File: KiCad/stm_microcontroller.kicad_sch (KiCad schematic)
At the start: 21 parts, among them J5 USB_C_Receptacle_USB2.0_14P, SW1 SW_Push, SW2 SW_Push, U1 STM32F103C8Tx, Y1 8Mhz

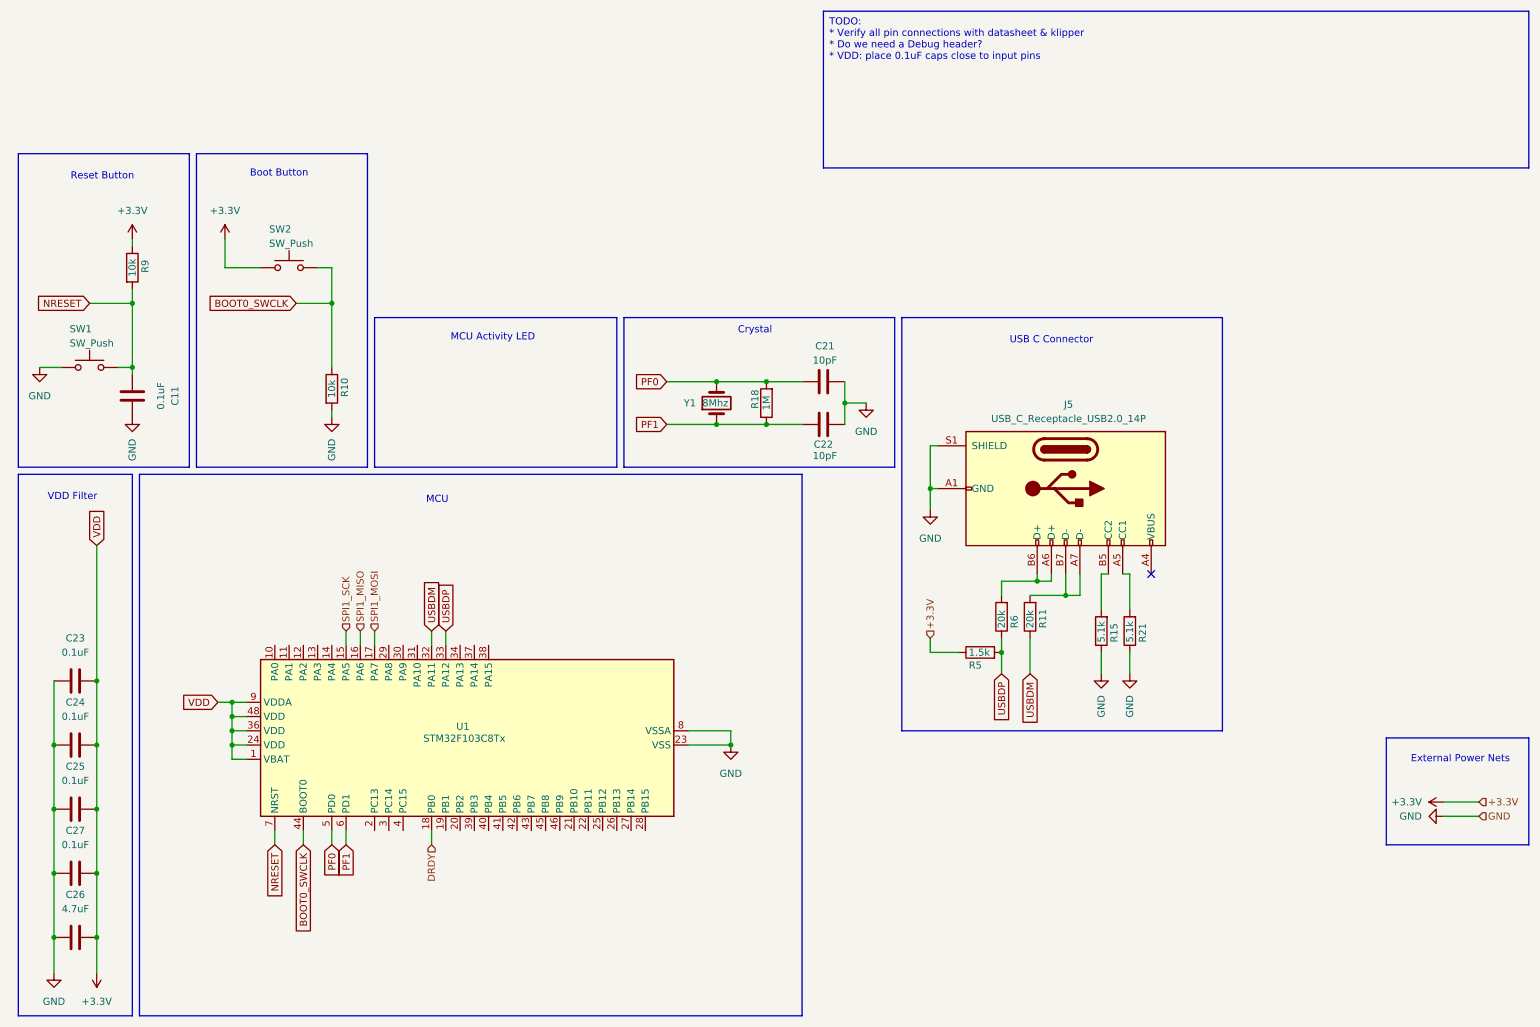
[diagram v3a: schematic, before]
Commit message: Update Switch Footprints
Update switch schematic and footprint to match the actual part being used
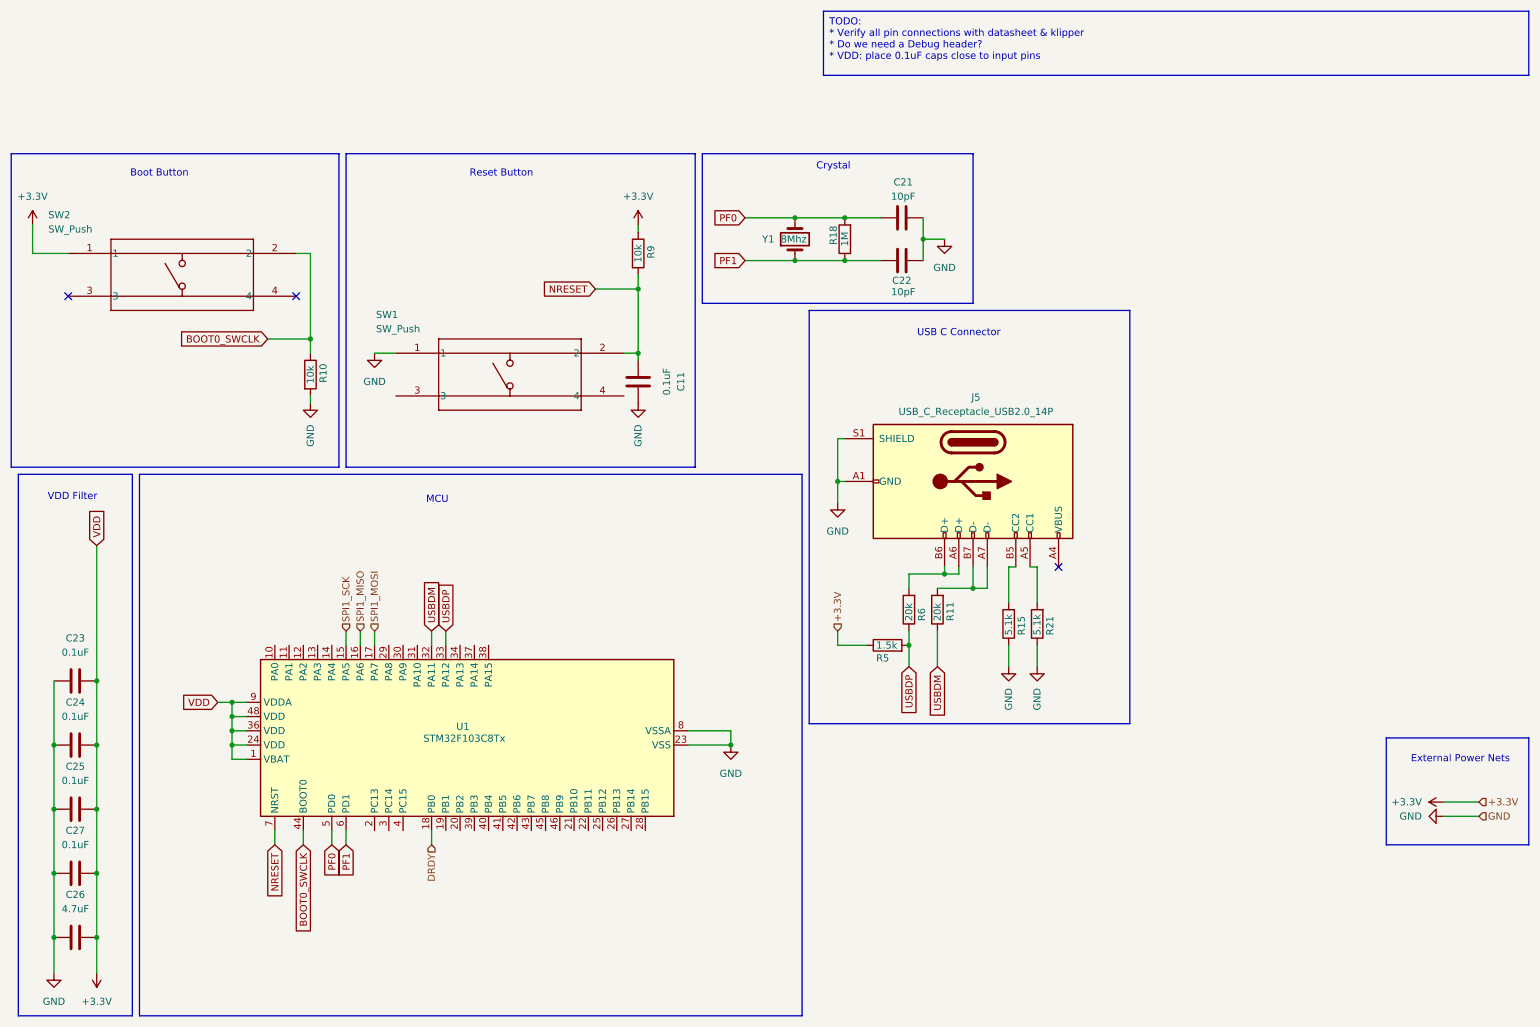
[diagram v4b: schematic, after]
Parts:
- J5: footprint Connector_USB:USB_C_Receptacle_GCT_USB4110 -> Connector_USB:USB_C_Receptacle_GCT_USB4085
- SW1, SW2: footprint Button_Switch_SMD:SW_Push_1P1T_NO_6x6mm_H9.5mm -> SWITCH_43SMTR92LFS; symbol Switch:SW_Push -> PTS645 Switch:PTS645SM43SMTR92LFS
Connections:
- no-connect marks 1 -> 3
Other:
- note removed: "MCU Activity LED"
- moved on the sheet: C11, C21, C22, J5, R10, R11, R15, R18, R21, R5, R6, R9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

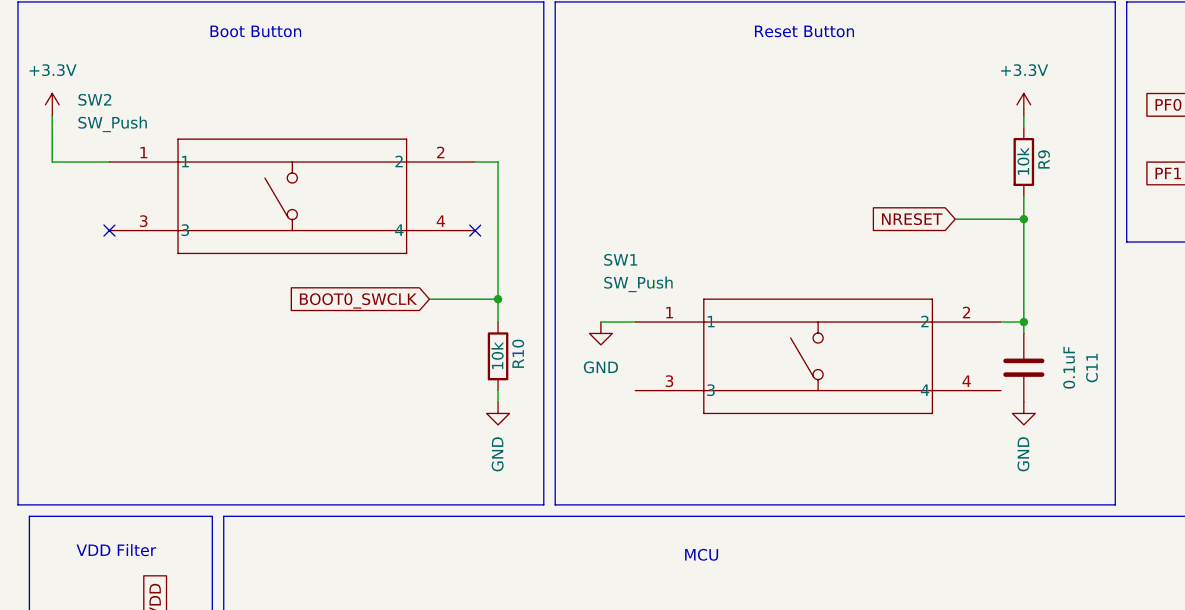
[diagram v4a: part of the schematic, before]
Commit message: Update Inductor Footprint
Update to PA4332.222NLT
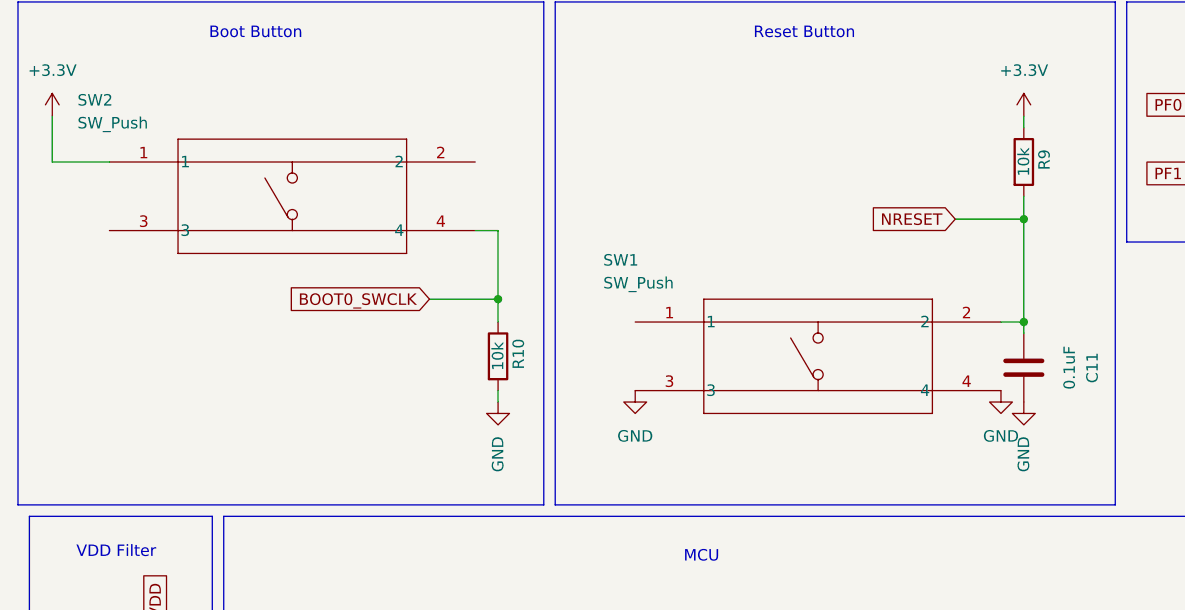
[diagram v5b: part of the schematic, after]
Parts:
- Y1: footprint Crystal:Crystal_SMD_SeikoEpson_FA238V-4Pin_3.2x2.5mm_HandSoldering -> Crystal:Crystal_SMD_Abracon_ABM3-2Pin_5.0x3.2mm
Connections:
- net BOOT0_SWCLK: now also SW2.4; no longer SW2.2
- net GND: now also SW1.3, SW1.4; no longer SW1.1
- no-connect marks 3 -> 1
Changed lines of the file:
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@@
 	)
 	(no_connect
-		(at 63.5 64.77)
-	)
-	(no_connect
-		(at 22.86 64.77)
-	)
-	(no_connect
 		(at 199.39 113.03)
 	)
@@
 	(wire
 		(pts
-			(xy 63.5 57.15) (xy 66.04 57.15)
+			(xy 63.5 64.77) (xy 66.04 64.77)
 		)
 		(stroke
@@
 	(wire
 		(pts
-			(xy 66.04 57.15) (xy 66.04 72.39)
+			(xy 66.04 64.77) (xy 66.04 72.39)
 		)
 		(stroke
@@
 	(wire
 		(pts
-			(xy 77.47 74.93) (xy 81.28 74.93)
-		)
-		(stroke
-			(width 0)
-			(type default)
-		)
-	)
-	(wire
-		(pts
 			(xy 52.07 137.16) (xy 52.07 139.7)
 		)
@@
 	)
 	(symbol
+		(lib_id "power:GND")
+		(at 121.92 82.55 0)
+		(unit 1)
+		(exclude_from_sim no)
+		(in_bom yes)
+		(on_board yes)
+		(dnp no)
+		(fields_autoplaced yes)
+		(property "Reference" "#PWR02"
+			(at 121.92 88.9 0)
+			(effects
+				(font
+					(size 1.27 1.27)
+				)
+				(hide yes)
+			)
+		)
+		(property "Value" "GND"
+			(at 121.92 87.63 0)
+			(effects
+				(font
+					(size 1.27 1.27)
+				)
+			)
+		)
+		(property "Footprint" ""
+			(at 121.92 82.55 0)
+			(effects
+				(font
+					(size 1.27 1.27)
+				)
+				(hide yes)
+			)
+		)
+		(property "Datasheet" ""
+			(at 121.92 82.55 0)
+			(effects
+				(font
+					(size 1.27 1.27)
+				)
+				(hide yes)
+			)
+		)
+		(property "Description" "Power symbol creates a global label with name \"GND\" , ground"
+			(at 121.92 82.55 0)
+			(effects
+				(font
+					(size 1.27 1.27)
+				)
+				(hide yes)
+			)
+		)
+		(pin "1"
+		)
+		(instances
+			(project "ADS1220 4-Load Cell Board"
+				(path "/5d164854-6659-4076-ba4e-df0771b4723d/50dff8a5-558b-4d50-9ac6-b993f14c2b34"
+					(reference "#PWR02")
+					(unit 1)
+				)
+			)
+		)
+	)
+	(symbol
 		(lib_id "Connector:USB_C_Receptacle_USB2.0_14P")
 		(at 184.15 97.79 270)
@@
 	(symbol
 		(lib_id "power:GND")
-		(at 77.47 74.93 0)
+		(at 81.28 82.55 0)
 		(unit 1)
 		(exclude_from_sim no)
@@
 		(fields_autoplaced yes)
 		(property "Reference" "#PWR025"
-			(at 77.47 81.28 0)
+			(at 81.28 88.9 0)
 			(effects
 				(font
@@
 		)
 		(property "Value" "GND"
-			(at 77.47 80.01 0)
+			(at 81.28 87.63 0)
 			(effects
 				(font
@@
 		)
 		(property "Footprint" ""
-			(at 77.47 74.93 0)
+			(at 81.28 82.55 0)
 			(effects
 				(font
@@
 		)
 		(property "Datasheet" ""
-			(at 77.47 74.93 0)
+			(at 81.28 82.55 0)
 			(effects
 				(font
@@
 		)
 		(property "Description" "Power symbol creates a global label with name \"GND\" , ground"
-			(at 77.47 74.93 0)
+			(at 81.28 82.55 0)
 			(effects
 				(font
@@
 			)
 		)
-		(property "Footprint" "Crystal:Crystal_SMD_SeikoEpson_FA238V-4Pin_3.2x2.5mm_HandSoldering"
+		(property "Footprint" "Crystal:Crystal_SMD_Abracon_ABM3-2Pin_5.0x3.2mm"
 			(at 152.4 54.61 0)
 			(effects

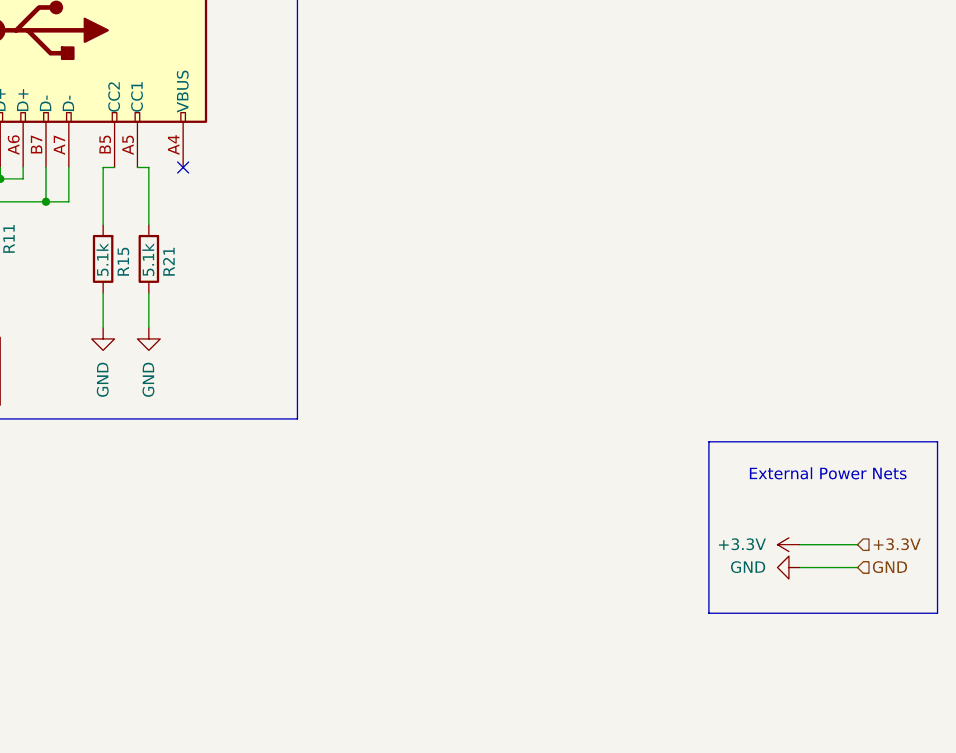
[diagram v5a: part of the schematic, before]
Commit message: Convert Power to LDOs
Convert power section to use only LDOs. This means we will only get 4.75V or 4.5V on the analog line but this comes with greatly increased simplicity of layout.
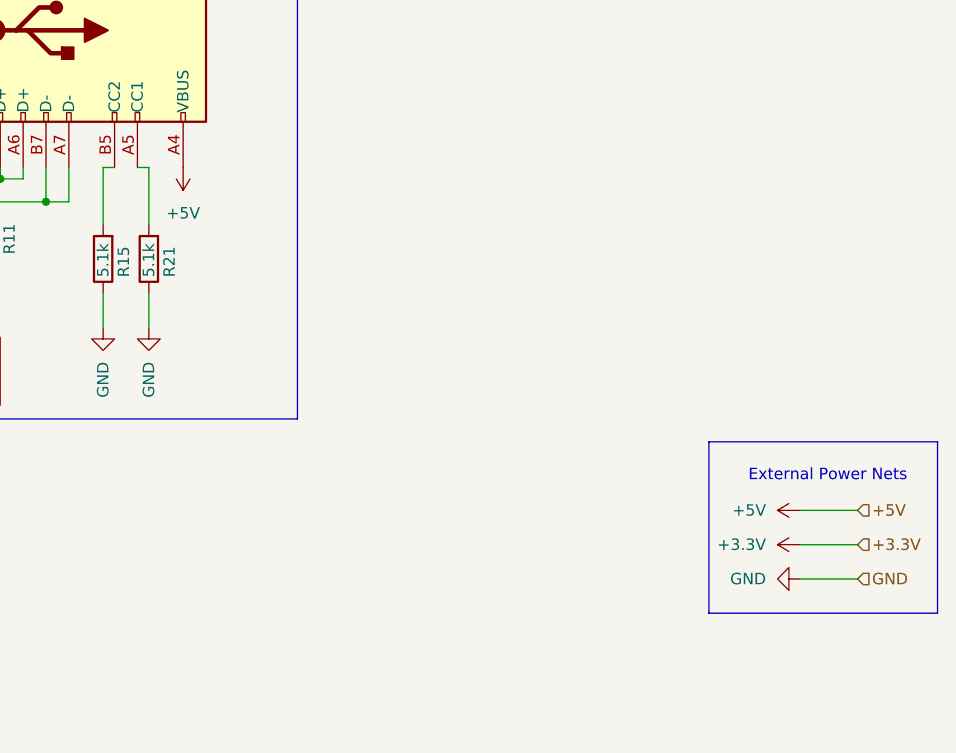
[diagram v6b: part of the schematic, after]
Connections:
- net +5V: now reaches J5.A4 (VBUS), J5.A9 (VBUS), J5.B4 (VBUS), J5.B9 (VBUS)
- no-connect marks 1 -> 0
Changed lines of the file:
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@@
 		(color 0 0 0 0)
 	)
-	(no_connect
-		(at 199.39 113.03)
-	)
 	(wire
 		(pts
@@
 	(wire
 		(pts
+			(xy 267.97 151.13) (xy 274.32 151.13)
+		)
+		(stroke
+			(width 0)
+			(type default)
+		)
+	)
+	(wire
+		(pts
 			(xy 267.97 154.94) (xy 274.32 154.94)
 		)
@@
 	(wire
 		(pts
-			(xy 267.97 157.48) (xy 274.32 157.48)
+			(xy 267.97 158.75) (xy 274.32 158.75)
 		)
 		(stroke
@@
 		)
 	)
+	(hierarchical_label "+5V"
+		(shape input)
+		(at 274.32 151.13 0)
+		(fields_autoplaced yes)
+		(effects
+			(font
+				(size 1.27 1.27)
+			)
+			(justify left)
+		)
+	)
 	(hierarchical_label "SPI1_MOSI"
 		(shape input)
@@
 	(hierarchical_label "GND"
 		(shape input)
-		(at 274.32 157.48 0)
+		(at 274.32 158.75 0)
 		(fields_autoplaced yes)
 		(effects
@@
 	(symbol
 		(lib_id "power:GND")
-		(at 267.97 157.48 270)
+		(at 267.97 158.75 270)
 		(unit 1)
 		(exclude_from_sim no)
@@
 		(fields_autoplaced yes)
 		(property "Reference" "#PWR015"
-			(at 261.62 157.48 0)
+			(at 261.62 158.75 0)
 			(effects
 				(font
@@
 		)
 		(property "Value" "GND"
-			(at 264.16 157.4799 90)
+			(at 264.16 158.7499 90)
 			(effects
 				(font
@@
 		)
 		(property "Footprint" ""
-			(at 267.97 157.48 0)
+			(at 267.97 158.75 0)
 			(effects
 				(font
@@
 		)
 		(property "Datasheet" ""
-			(at 267.97 157.48 0)
+			(at 267.97 158.75 0)
 			(effects
 				(font
@@
 		)
 		(property "Description" "Power symbol creates a global label with name \"GND\" , ground"
-			(at 267.97 157.48 0)
+			(at 267.97 158.75 0)
 			(effects
 				(font
@@
 	)
 	(symbol
+		(lib_id "power:+5V")
+		(at 267.97 151.13 90)
+		(unit 1)
+		(exclude_from_sim no)
+		(in_bom yes)
+		(on_board yes)
+		(dnp no)
+		(fields_autoplaced yes)
+		(property "Reference" "#PWR07"
+			(at 271.78 151.13 0)
+			(effects
+				(font
+					(size 1.27 1.27)
+				)
+				(hide yes)
+			)
+		)
+		(property "Value" "+5V"
+			(at 264.16 151.1299 90)
+			(effects
+				(font
+					(size 1.27 1.27)
+				)
+				(justify left)
+			)
+		)
+		(property "Footprint" ""
+			(at 267.97 151.13 0)
+			(effects
+				(font
+					(size 1.27 1.27)
+				)
+				(hide yes)
+			)
+		)
+		(property "Datasheet" ""
+			(at 267.97 151.13 0)
+			(effects
+				(font
+					(size 1.27 1.27)
+				)
+				(hide yes)
+			)
+		)
+		(property "Description" "Power symbol creates a global label with name \"+5V\""
+			(at 267.97 151.13 0)
+			(effects
+				(font
+					(size 1.27 1.27)
+				)
+				(hide yes)
+			)
+		)
+		(pin "1"
+		)
+		(instances
+			(project ""
+				(path "/5d164854-6659-4076-ba4e-df0771b4723d/50dff8a5-558b-4d50-9ac6-b993f14c2b34"
+					(reference "#PWR07")
+					(unit 1)
+				)
+			)
+		)
+	)
+	(symbol
 		(lib_id "power:GND")
 		(at 81.28 82.55 0)
@@
 					(unit 1)
 				)
+			)
+		)
+	)
+	(symbol
+		(lib_id "power:+5V")
+		(at 199.39 113.03 180)
+		(unit 1)
+		(exclude_from_sim no)
+		(in_bom yes)
+		(on_board yes)
+		(dnp no)
+		(fields_autoplaced yes)
+		(property "Reference" "#PWR018"
+			(at 199.39 109.22 0)
+			(effects
+				(font
+					(size 1.27 1.27)
+				)
+				(hide yes)
+			)
+		)
+		(property "Value" "+5V"
+			(at 199.39 118.11 0)
+			(effects
+				(font
+					(size 1.27 1.27)
+				)
+			)
+		)
+		(property "Footprint" ""
+			(at 199.39 113.03 0)
+			(effects
+				(font
+					(size 1.27 1.27)
+				)
+				(hide yes)
+			)
+		)
+		(property "Datasheet" ""
+			(at 199.39 113.03 0)
+			(effects
+				(font
+					(size 1.27 1.27)
+				)
+				(hide yes)
+			)
+		)
+		(property "Description" "Power symbol creates a global label with name \"+5V\""
+			(at 199.39 113.03 0)
+			(effects
+				(font
+					(size 1.27 1.27)
+				)
+				(hide yes)
+			)
+		)
+		(pin "1"
+		)
+		(instances
+			(project "ADS1220 4-Load Cell Board"
+				(path "/5d164854-6659-4076-ba4e-df0771b4723d/50dff8a5-558b-4d50-9ac6-b993f14c2b34"
+					(reference "#PWR018")
+					(unit 1)
+				)
